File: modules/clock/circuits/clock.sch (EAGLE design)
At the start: 32 parts, among them IC1 4056N, IC2 4056N, IC3 4056N

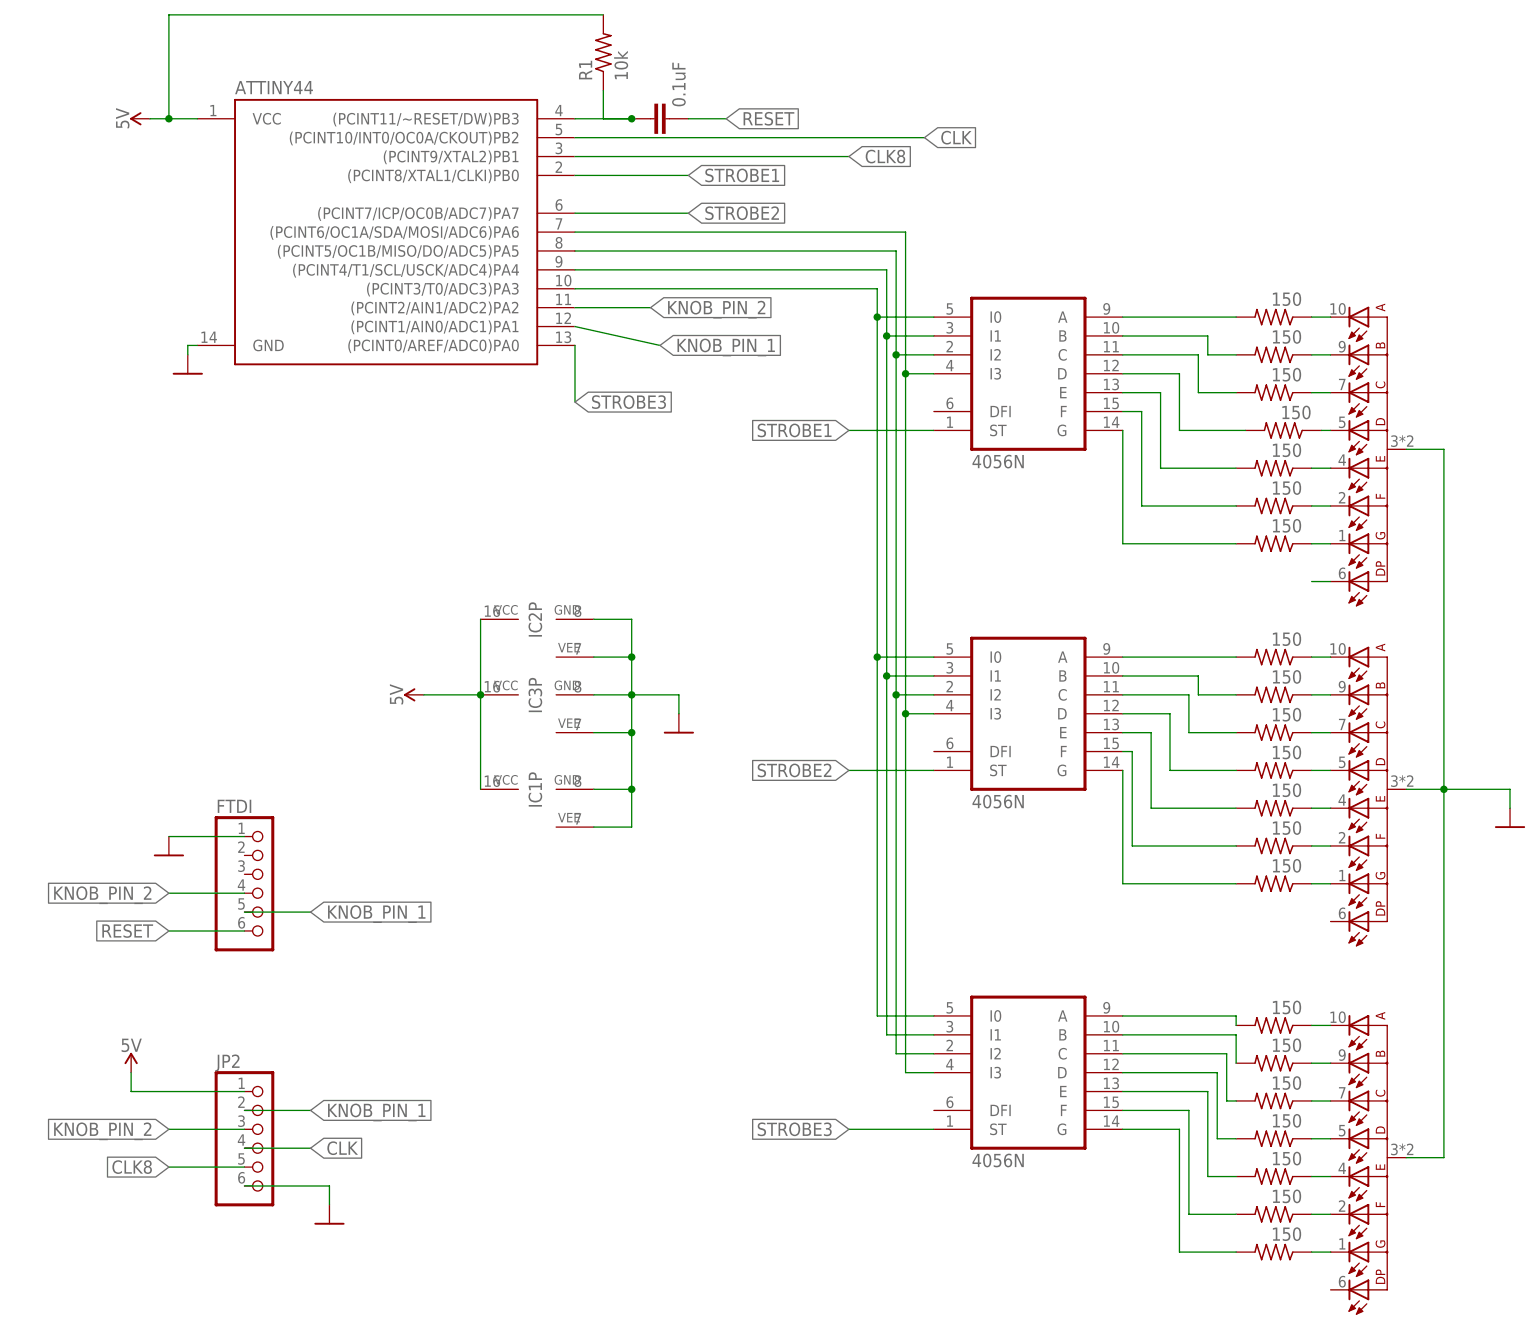
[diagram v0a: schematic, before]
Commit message: PCB correction for clock
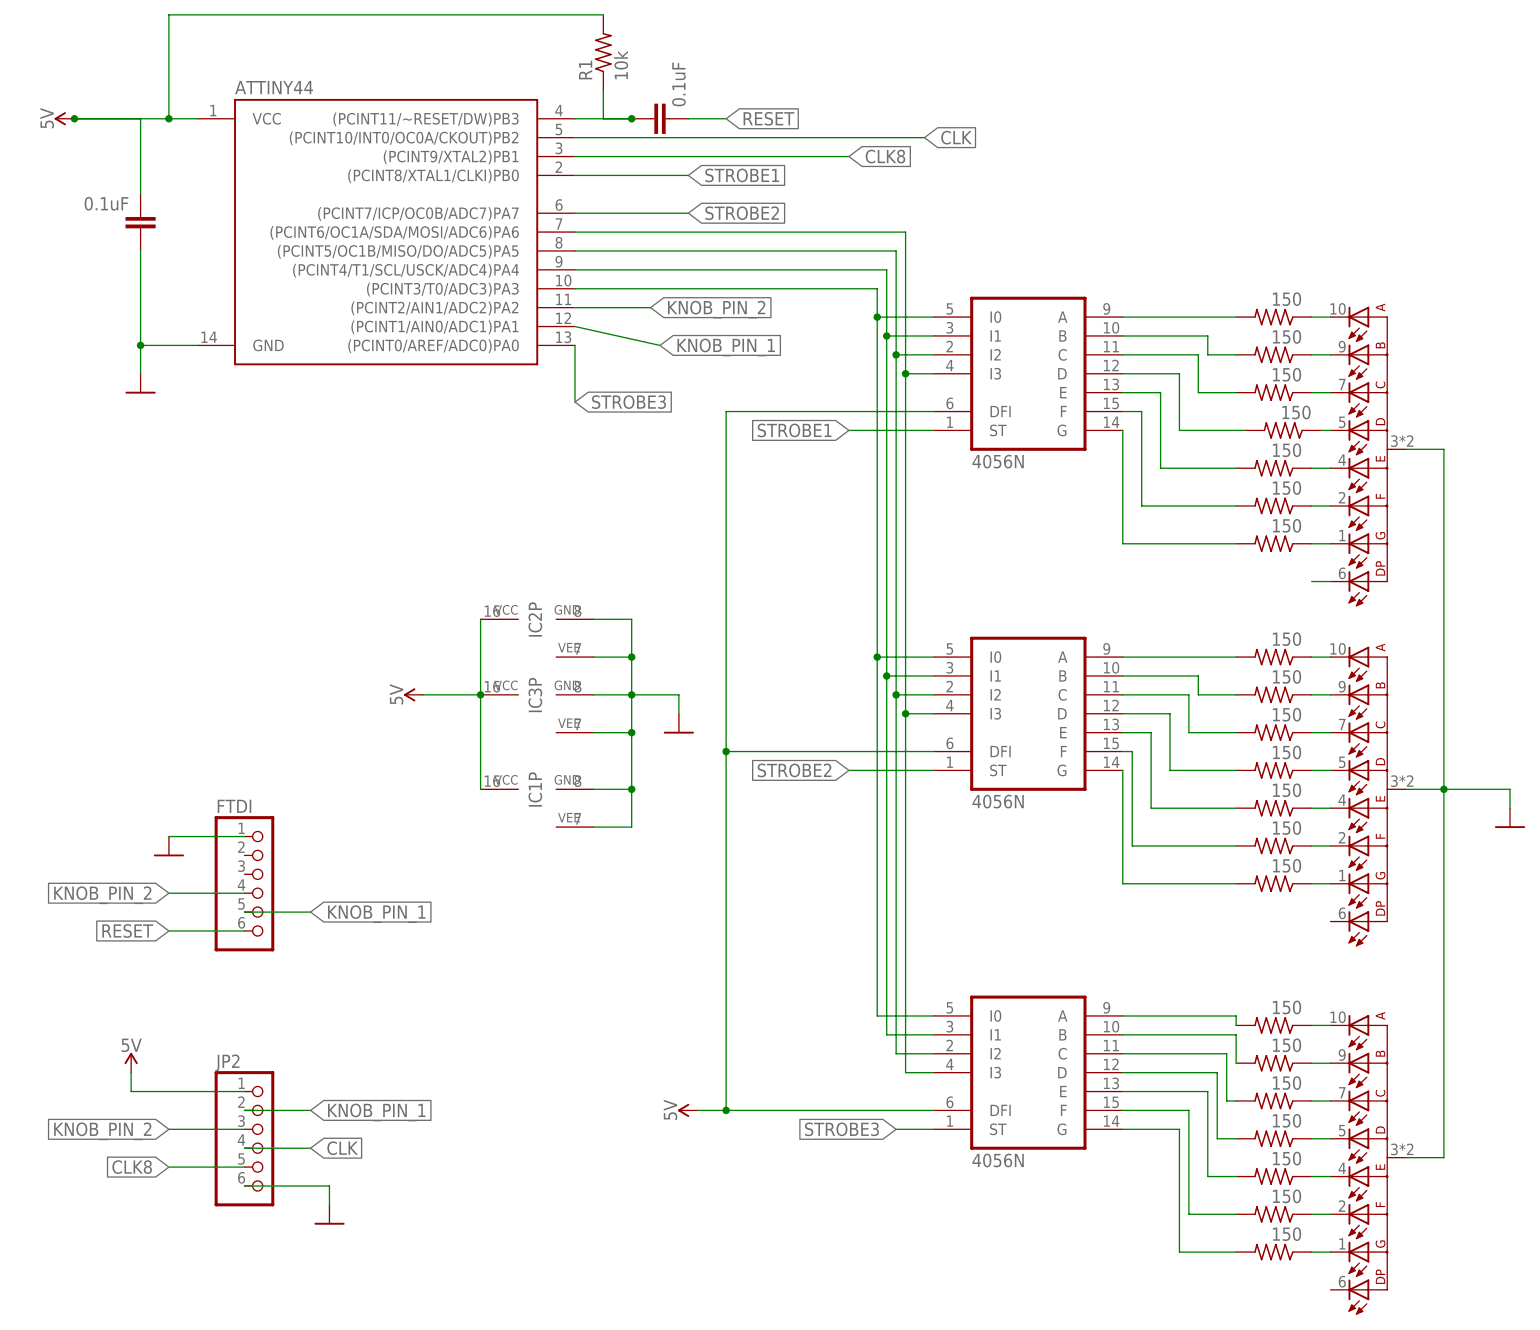
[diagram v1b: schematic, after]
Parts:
- added C3: 0.1uF, SparkFun-Capacitors:0.1UF-KIT-EZ-50V-20%
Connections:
- net 5V: now also C3.2, IC1A.DFI, IC2A.DFI, IC3A.DFI
- net GND: now also C3.1
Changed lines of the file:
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@@
 <setting verticaltext="up"/>
 </settings>
-<grid distance="0.1" unitdist="inch" unit="inch" style="lines" multiple="1" display="no" altdistance="0.01" altunitdist="inch" altunit="inch"/>
+<grid distance="0.05" unitdist="inch" unit="inch" style="lines" multiple="1" display="yes" altdistance="0.01" altunitdist="inch" altunit="inch"/>
 <layers>
 <layer number="1" name="Top" color="4" fill="1" visible="no" active="no"/>
@@
 <part name="R23" library="adafruit" library_urn="urn:adsk.eagle:library:420" deviceset="R-US_" device="0207/12" package3d_urn="urn:adsk.eagle:package:6240598/1" value="150"/>
 <part name="R24" library="adafruit" library_urn="urn:adsk.eagle:library:420" deviceset="R-US_" device="0207/12" package3d_urn="urn:adsk.eagle:package:6240598/1" value="150"/>
+<part name="C3" library="SparkFun-Capacitors" library_urn="urn:adsk.eagle:library:510" deviceset="0.1UF" device="-KIT-EZ-50V-20%" package3d_urn="urn:adsk.eagle:package:37428/1" value="0.1uF"/>
+<part name="SUPPLY4" library="SparkFun-PowerSymbols" library_urn="urn:adsk.eagle:library:530" deviceset="5V" device=""/>
 </parts>
 <sheets>
@@
 </instance>
 <instance part="GND2" gate="1" x="60.96" y="-21.59" smashed="yes"/>
-<instance part="GND3" gate="1" x="63.5" y="43.18" smashed="yes"/>
-<instance part="SUPPLY2" gate="G$1" x="58.42" y="77.47" smashed="yes" rot="R90">
-<attribute name="VALUE" x="55.626" y="77.47" size="1.778" layer="96" rot="R90" align="bottom-center"/>
+<instance part="GND3" gate="1" x="57.15" y="40.64" smashed="yes"/>
+<instance part="SUPPLY2" gate="G$1" x="48.26" y="77.47" smashed="yes" rot="R90">
+<attribute name="VALUE" x="45.466" y="77.47" size="1.778" layer="96" rot="R90" align="bottom-center"/>
 </instance>
 <instance part="C2" gate="G$1" x="128.27" y="77.47" smashed="yes" rot="R90">
@@
 <attribute name="VALUE" x="213.36" y="-71.628" size="1.778" layer="96" rot="R180"/>
 </instance>
+<instance part="C3" gate="G$1" x="57.15" y="64.77" smashed="yes" rot="R180">
+<attribute name="VALUE" x="55.626" y="66.929" size="1.778" layer="96" font="vector" rot="R180"/>
+</instance>
+<instance part="SUPPLY4" gate="G$1" x="132.08" y="-55.88" smashed="yes" rot="R90">
+<attribute name="VALUE" x="129.286" y="-55.88" size="1.778" layer="96" rot="R90" align="bottom-center"/>
+</instance>
 </instances>
 <busses>
@@
 <pinref part="SUPPLY2" gate="G$1" pin="5V"/>
 <pinref part="ATTINY44" gate="G$1" pin="VCC"/>
-<wire x1="58.42" y1="77.47" x2="60.96" y2="77.47" width="0.1524" layer="91"/>
+<wire x1="48.26" y1="77.47" x2="60.96" y2="77.47" width="0.1524" layer="91"/>
 <pinref part="R1" gate="G$1" pin="2"/>
 <wire x1="60.96" y1="77.47" x2="64.77" y2="77.47" width="0.1524" layer="91"/>
@@
 <wire x1="60.96" y1="91.44" x2="60.96" y2="77.47" width="0.1524" layer="91"/>
 <junction x="60.96" y="77.47"/>
+<pinref part="C3" gate="G$1" pin="2"/>
+<wire x1="48.26" y1="77.47" x2="57.15" y2="77.47" width="0.1524" layer="91"/>
+<wire x1="57.15" y1="77.47" x2="57.15" y2="67.31" width="0.1524" layer="91"/>
+<junction x="48.26" y="77.47"/>
 </segment>
 <segment>
@@
 <pinref part="SUPPLY3" gate="G$1" pin="5V"/>
 </segment>
+<segment>
+<pinref part="IC1" gate="A" pin="DFI"/>
+<wire x1="163.83" y1="-55.88" x2="135.89" y2="-55.88" width="0.1524" layer="91"/>
+<pinref part="SUPPLY4" gate="G$1" pin="5V"/>
+<pinref part="IC2" gate="A" pin="DFI"/>
+<wire x1="135.89" y1="-55.88" x2="132.08" y2="-55.88" width="0.1524" layer="91"/>
+<wire x1="163.83" y1="38.1" x2="135.89" y2="38.1" width="0.1524" layer="91"/>
+<pinref part="IC3" gate="A" pin="DFI"/>
+<wire x1="135.89" y1="38.1" x2="135.89" y2="-7.62" width="0.1524" layer="91"/>
+<wire x1="135.89" y1="-7.62" x2="163.83" y2="-7.62" width="0.1524" layer="91"/>
+<wire x1="135.89" y1="-7.62" x2="135.89" y2="-55.88" width="0.1524" layer="91"/>
+<junction x="135.89" y="-7.62"/>
+<junction x="135.89" y="-55.88"/>
+</segment>
 </net>
 <net name="GND" class="0">
@@
 <pinref part="GND2" gate="1" pin="GND"/>
 <wire x1="71.12" y1="-19.05" x2="60.96" y2="-19.05" width="0.1524" layer="91"/>
-</segment>
-<segment>
-<pinref part="GND3" gate="1" pin="GND"/>
-<wire x1="63.5" y1="45.72" x2="63.5" y2="46.99" width="0.1524" layer="91"/>
-<pinref part="ATTINY44" gate="G$1" pin="GND"/>
-<wire x1="63.5" y1="46.99" x2="64.77" y2="46.99" width="0.1524" layer="91"/>
 </segment>
 <segment>
@@
 <pinref part="GND4" gate="1" pin="GND"/>
 </segment>
+<segment>
+<pinref part="ATTINY44" gate="G$1" pin="GND"/>
+<pinref part="GND3" gate="1" pin="GND"/>
+<wire x1="64.77" y1="46.99" x2="57.15" y2="46.99" width="0.1524" layer="91"/>
+<pinref part="C3" gate="G$1" pin="1"/>
+<wire x1="57.15" y1="46.99" x2="57.15" y2="43.18" width="0.1524" layer="91"/>
+<wire x1="57.15" y1="46.99" x2="57.15" y2="59.69" width="0.1524" layer="91"/>
+<junction x="57.15" y="46.99"/>
+</segment>
 </net>
 <net name="RESET" class="0">
@@
 <segment>
 <pinref part="IC1" gate="A" pin="ST"/>
-<wire x1="163.83" y1="-58.42" x2="152.4" y2="-58.42" width="0.1524" layer="91"/>
-<label x="152.4" y="-58.42" size="1.778" layer="95" rot="R180" xref="yes"/>
+<wire x1="163.83" y1="-58.42" x2="158.75" y2="-58.42" width="0.1524" layer="91"/>
+<label x="158.75" y="-58.42" size="1.778" layer="95" rot="R180" xref="yes"/>
 </segment>
 <segment>
@@
 </sheet>
 </sheets>
-<errors>
-</errors>
 </schematic>
 </drawing>

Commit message: midi2cv
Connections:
- net 5V: now also D1.+, D2.+, D3.+
- net GND: no longer D1.+, D2.+, D3.+
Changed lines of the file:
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@@
 <?xml version="1.0" encoding="utf-8"?>
 <!DOCTYPE eagle SYSTEM "eagle.dtd">
-<eagle version="9.5.2">
+<eagle version="9.6.2">
 <drawing>
 <settings>
@@
 <setting verticaltext="up"/>
 </settings>
-<grid distance="0.05" unitdist="inch" unit="inch" style="lines" multiple="1" display="yes" altdistance="0.01" altunitdist="inch" altunit="inch"/>
+<grid distance="0.1" unitdist="inch" unit="inch" style="lines" multiple="1" display="no" altdistance="0.01" altunitdist="inch" altunit="inch"/>
 <layers>
 <layer number="1" name="Top" color="4" fill="1" visible="no" active="no"/>
@@
 <part name="SUPPLY2" library="SparkFun-PowerSymbols" library_urn="urn:adsk.eagle:library:530" deviceset="5V" device=""/>
 <part name="C2" library="SparkFun-Capacitors" library_urn="urn:adsk.eagle:library:510" deviceset="0.1UF" device="-KIT-EZ-50V-20%" package3d_urn="urn:adsk.eagle:package:37428/1" value="0.1uF"/>
-<part name="GND4" library="supply1" library_urn="urn:adsk.eagle:library:371" deviceset="GND" device=""/>
 <part name="R1" library="adafruit" library_urn="urn:adsk.eagle:library:420" deviceset="R-US_" device="0207/12" package3d_urn="urn:adsk.eagle:package:6240598/1" value="10k"/>
 <part name="R2" library="adafruit" library_urn="urn:adsk.eagle:library:420" deviceset="R-US_" device="0207/12" package3d_urn="urn:adsk.eagle:package:6240598/1" value="150"/>
@@
 <part name="C3" library="SparkFun-Capacitors" library_urn="urn:adsk.eagle:library:510" deviceset="0.1UF" device="-KIT-EZ-50V-20%" package3d_urn="urn:adsk.eagle:package:37428/1" value="0.1uF"/>
 <part name="SUPPLY4" library="SparkFun-PowerSymbols" library_urn="urn:adsk.eagle:library:530" deviceset="5V" device=""/>
+<part name="SUPPLY5" library="SparkFun-PowerSymbols" library_urn="urn:adsk.eagle:library:530" deviceset="5V" device=""/>
 </parts>
 <sheets>
@@
 <attribute name="VALUE" x="130.429" y="78.994" size="1.778" layer="96" font="vector" rot="R90"/>
 </instance>
-<instance part="GND4" gate="1" x="241.3" y="-17.78" smashed="yes"/>
 <instance part="R1" gate="G$1" x="119.38" y="86.36" smashed="yes" rot="R90">
 <attribute name="NAME" x="117.8814" y="82.55" size="1.778" layer="95" rot="R90"/>
@@
 <instance part="SUPPLY4" gate="G$1" x="132.08" y="-55.88" smashed="yes" rot="R90">
 <attribute name="VALUE" x="129.286" y="-55.88" size="1.778" layer="96" rot="R90" align="bottom-center"/>
+</instance>
+<instance part="SUPPLY5" gate="G$1" x="241.3" y="-7.62" smashed="yes">
+<attribute name="VALUE" x="241.3" y="-4.826" size="1.778" layer="96" align="bottom-center"/>
 </instance>
 </instances>
@@
 <junction x="135.89" y="-7.62"/>
 <junction x="135.89" y="-55.88"/>
+</segment>
+<segment>
+<pinref part="D2" gate="G$1" pin="+"/>
+<wire x1="227.33" y1="-62.23" x2="232.41" y2="-62.23" width="0.1524" layer="91"/>
+<wire x1="232.41" y1="-62.23" x2="232.41" y2="-12.7" width="0.1524" layer="91"/>
+<pinref part="D3" gate="G$1" pin="+"/>
+<wire x1="232.41" y1="-12.7" x2="227.33" y2="-12.7" width="0.1524" layer="91"/>
+<pinref part="D1" gate="G$1" pin="+"/>
+<wire x1="227.33" y1="33.02" x2="232.41" y2="33.02" width="0.1524" layer="91"/>
+<wire x1="232.41" y1="33.02" x2="232.41" y2="-12.7" width="0.1524" layer="91"/>
+<junction x="232.41" y="-12.7"/>
+<wire x1="232.41" y1="-12.7" x2="241.3" y2="-12.7" width="0.1524" layer="91"/>
+<pinref part="SUPPLY5" gate="G$1" pin="5V"/>
+<wire x1="241.3" y1="-7.62" x2="241.3" y2="-12.7" width="0.1524" layer="91"/>
 </segment>
 </net>
@@
 </segment>
 <segment>
-<pinref part="D2" gate="G$1" pin="+"/>
-<wire x1="227.33" y1="-62.23" x2="232.41" y2="-62.23" width="0.1524" layer="91"/>
-<wire x1="232.41" y1="-62.23" x2="232.41" y2="-12.7" width="0.1524" layer="91"/>
-<pinref part="D3" gate="G$1" pin="+"/>
-<wire x1="232.41" y1="-12.7" x2="227.33" y2="-12.7" width="0.1524" layer="91"/>
-<pinref part="D1" gate="G$1" pin="+"/>
-<wire x1="227.33" y1="33.02" x2="232.41" y2="33.02" width="0.1524" layer="91"/>
-<wire x1="232.41" y1="33.02" x2="232.41" y2="-12.7" width="0.1524" layer="91"/>
-<junction x="232.41" y="-12.7"/>
-<wire x1="232.41" y1="-12.7" x2="241.3" y2="-12.7" width="0.1524" layer="91"/>
-<wire x1="241.3" y1="-12.7" x2="241.3" y2="-15.24" width="0.1524" layer="91"/>
-<pinref part="GND4" gate="1" pin="GND"/>
-</segment>
-<segment>
